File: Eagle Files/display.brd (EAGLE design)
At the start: 38.4 x 51.4 mm, 16 parts, among them CN1 Charger, IC1 ATMEGA 328P-PU

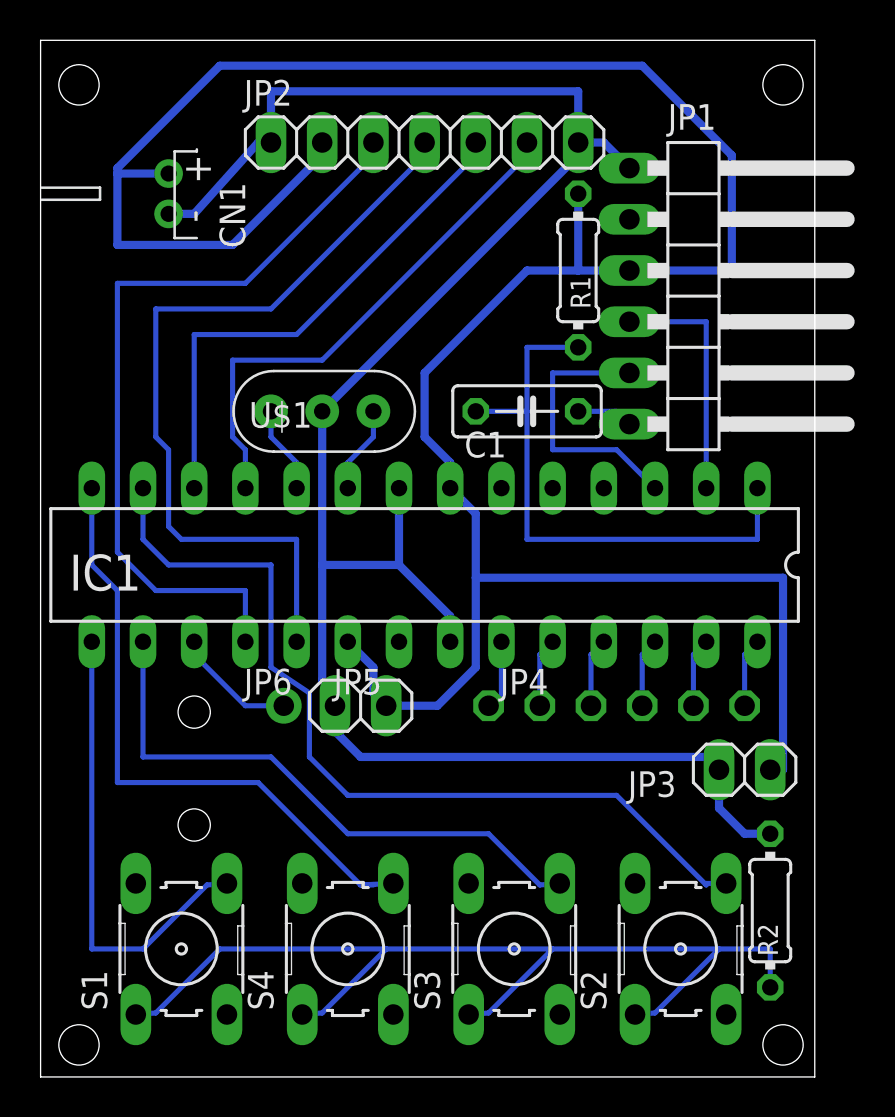
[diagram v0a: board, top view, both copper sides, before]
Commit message: removed one button
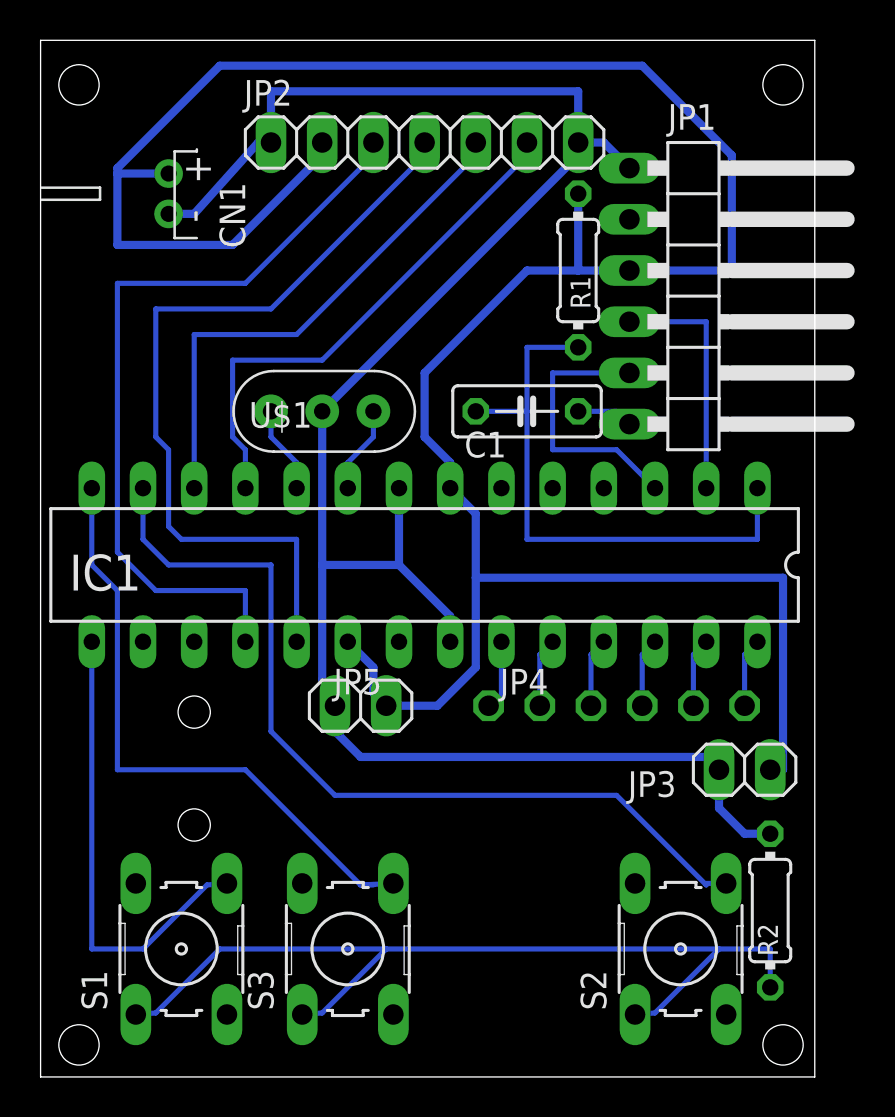
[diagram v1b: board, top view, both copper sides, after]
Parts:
- removed JP6: PWM, adafruit:1X01-CLEANBIG
- removed S4: (no value), switch-omron:B3F-10XX
- moved S3 8.26 mm to (15.2, 6.35)
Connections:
- removed net N$23: IC1.17, JP6.1
- removed net N$9: IC1.16, S3.4
- net N$13: no longer S4.1
- net N$17: now also S3.4; no longer S4.4
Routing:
- net N$9: track 29.0 -> 0.00 mm
- net N$23: track 6.13 -> 0.00 mm
- net N$13: track 51.1 -> 45.7 mm
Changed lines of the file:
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@@
 <attribute name="OC_FARNELL" value="176432" x="31.75" y="6.35" size="1.778" layer="27" rot="R90" display="off"/>
-</element>
-<element name="S3" library="switch-omron" package="B3F-10XX" value="" x="23.495" y="6.35" rot="R90">
-<attribute name="OC_NEWARK" value="36M3542" x="23.495" y="6.35" size="1.778" layer="27" rot="R90" display="off"/>
-<attribute name="MPN" value="B3F-1000" x="23.495" y="6.35" size="1.778" layer="27" rot="R90" display="off"/>
-<attribute name="MF" value="" x="23.495" y="6.35" size="1.778" layer="27" rot="R90" display="off"/>
-<attribute name="OC_FARNELL" value="176432" x="23.495" y="6.35" size="1.778" layer="27" rot="R90" display="off"/>
 </element>
 <element name="R2" library="rcl" package="0204/7" value="100" x="36.195" y="8.255" smashed="yes" rot="R270">
@@
 <attribute name="VALUE" x="35.7124" y="10.5156" size="0.9906" layer="27" ratio="10" rot="R270"/>
 </element>
-<element name="S4" library="switch-omron" package="B3F-10XX" value="" x="15.24" y="6.35" rot="R90">
+<element name="S3" library="switch-omron" package="B3F-10XX" value="" x="15.24" y="6.35" rot="R90">
 <attribute name="OC_NEWARK" value="36M3542" x="15.24" y="6.35" size="1.778" layer="27" rot="R90" display="off"/>
 <attribute name="MPN" value="B3F-1000" x="15.24" y="6.35" size="1.778" layer="27" rot="R90" display="off"/>
@@
 <attribute name="NAME" x="22.7838" y="18.9738" size="1.27" layer="25" ratio="10"/>
 <attribute name="VALUE" x="21.59" y="15.875" size="1.27" layer="27"/>
-</element>
-<element name="JP6" library="adafruit" package="1X01-CLEANBIG" value="PWM" x="12.065" y="18.415" smashed="yes">
-<attribute name="NAME" x="10.0838" y="18.9738" size="1.27" layer="25" ratio="10"/>
-<attribute name="VALUE" x="9.525" y="15.875" size="1.27" layer="27"/>
 </element>
 </elements>
@@
 <signal name="N$11">
 <contactref element="S2" pad="4"/>
-<wire x1="15.24" y1="13.97" x2="13.335" y2="15.875" width="0.254" layer="16"/>
-<wire x1="13.335" y1="15.875" x2="13.335" y2="19.05" width="0.254" layer="16"/>
-<wire x1="13.335" y1="19.05" x2="11.43" y2="20.32" width="0.254" layer="16"/>
-<wire x1="11.43" y1="20.32" x2="11.43" y2="25.4" width="0.254" layer="16"/>
-<wire x1="28.575" y1="13.97" x2="15.24" y2="13.97" width="0.254" layer="16"/>
+<wire x1="14.605" y1="13.97" x2="11.43" y2="17.145" width="0.254" layer="16"/>
+<wire x1="11.43" y1="17.145" x2="11.43" y2="25.4" width="0.254" layer="16"/>
+<wire x1="28.575" y1="13.97" x2="14.605" y2="13.97" width="0.254" layer="16"/>
 <wire x1="33.02" y1="9.525" x2="28.575" y2="13.97" width="0.254" layer="16"/>
 <wire x1="33.02" y1="9.525" x2="33.02" y2="9.6012" width="0.254" layer="16"/>
@@
 <wire x1="6.35" y1="25.4" x2="5.08" y2="26.67" width="0.254" layer="16"/>
 <wire x1="5.08" y1="26.67" x2="5.08" y2="29.21" width="0.254" layer="16"/>
-</signal>
-<signal name="N$9">
-<contactref element="S3" pad="4"/>
-<contactref element="IC1" pad="16"/>
-<wire x1="24.765" y1="9.525" x2="22.225" y2="12.065" width="0.254" layer="16"/>
-<wire x1="24.765" y1="9.525" x2="25.7556" y2="9.6012" width="0.254" layer="16"/>
-<wire x1="22.225" y1="12.065" x2="15.24" y2="12.065" width="0.254" layer="16"/>
-<wire x1="15.24" y1="12.065" x2="11.43" y2="15.875" width="0.254" layer="16"/>
-<wire x1="11.43" y1="15.875" x2="5.08" y2="15.875" width="0.254" layer="16"/>
-<wire x1="5.08" y1="15.875" x2="5.08" y2="21.59" width="0.254" layer="16"/>
 </signal>
 <signal name="N$4">
@@
 </signal>
 <signal name="N$13">
-<contactref element="S3" pad="1"/>
 <contactref element="R2" pad="2"/>
 <contactref element="S1" pad="1"/>
 <contactref element="S2" pad="1"/>
-<contactref element="S4" pad="1"/>
+<contactref element="S3" pad="1"/>
 <wire x1="17.145" y1="6.35" x2="13.97" y2="3.175" width="0.254" layer="16"/>
 <wire x1="13.97" y1="3.175" x2="12.9794" y2="3.0988" width="0.254" layer="16"/>
@@
 <wire x1="30.48" y1="3.175" x2="33.655" y2="6.35" width="0.254" layer="16"/>
 <wire x1="30.48" y1="3.175" x2="29.4894" y2="3.0988" width="0.254" layer="16"/>
-<wire x1="25.4" y1="6.35" x2="22.225" y2="3.175" width="0.254" layer="16"/>
-<wire x1="33.655" y1="6.35" x2="25.4" y2="6.35" width="0.254" layer="16"/>
-<wire x1="22.225" y1="3.175" x2="21.2344" y2="3.0988" width="0.254" layer="16"/>
-<wire x1="25.4" y1="6.35" x2="17.145" y2="6.35" width="0.254" layer="16"/>
+<wire x1="33.655" y1="6.35" x2="17.145" y2="6.35" width="0.254" layer="16"/>
 <wire x1="17.145" y1="6.35" x2="8.89" y2="6.35" width="0.254" layer="16"/>
 <wire x1="8.89" y1="6.35" x2="5.715" y2="3.175" width="0.254" layer="16"/>
@@
 </signal>
 <signal name="N$17">
-<contactref element="S4" pad="4"/>
+<contactref element="S3" pad="4"/>
 <contactref element="IC1" pad="14"/>
 <wire x1="2.54" y1="25.4" x2="2.54" y2="29.21" width="0.254" layer="16"/>
-<wire x1="10.795" y1="14.605" x2="3.81" y2="14.605" width="0.254" layer="16"/>
-<wire x1="3.81" y1="14.605" x2="3.81" y2="24.13" width="0.254" layer="16"/>
+<wire x1="10.16" y1="15.24" x2="3.81" y2="15.24" width="0.254" layer="16"/>
+<wire x1="3.81" y1="15.24" x2="3.81" y2="24.13" width="0.254" layer="16"/>
 <wire x1="3.81" y1="24.13" x2="2.54" y2="25.4" width="0.254" layer="16"/>
 <wire x1="16.51" y1="9.525" x2="15.875" y2="9.525" width="0.254" layer="16"/>
-<wire x1="15.875" y1="9.525" x2="10.795" y2="14.605" width="0.254" layer="16"/>
+<wire x1="15.875" y1="9.525" x2="10.16" y2="15.24" width="0.254" layer="16"/>
 <wire x1="15.875" y1="9.525" x2="17.5006" y2="9.6012" width="0.254" layer="16"/>
 </signal>
@@
 <wire x1="24.765" y1="18.415" x2="24.765" y2="20.955" width="0.254" layer="16"/>
 </signal>
-<signal name="N$23">
-<contactref element="IC1" pad="17"/>
-<wire x1="12.065" y1="18.415" x2="10.16" y2="18.415" width="0.254" layer="16"/>
-<wire x1="10.16" y1="18.415" x2="7.62" y2="20.955" width="0.254" layer="16"/>
-<wire x1="7.62" y1="20.955" x2="7.62" y2="21.59" width="0.254" layer="16"/>
-<contactref element="JP6" pad="1"/>
-</signal>
 <signal name="N$24">

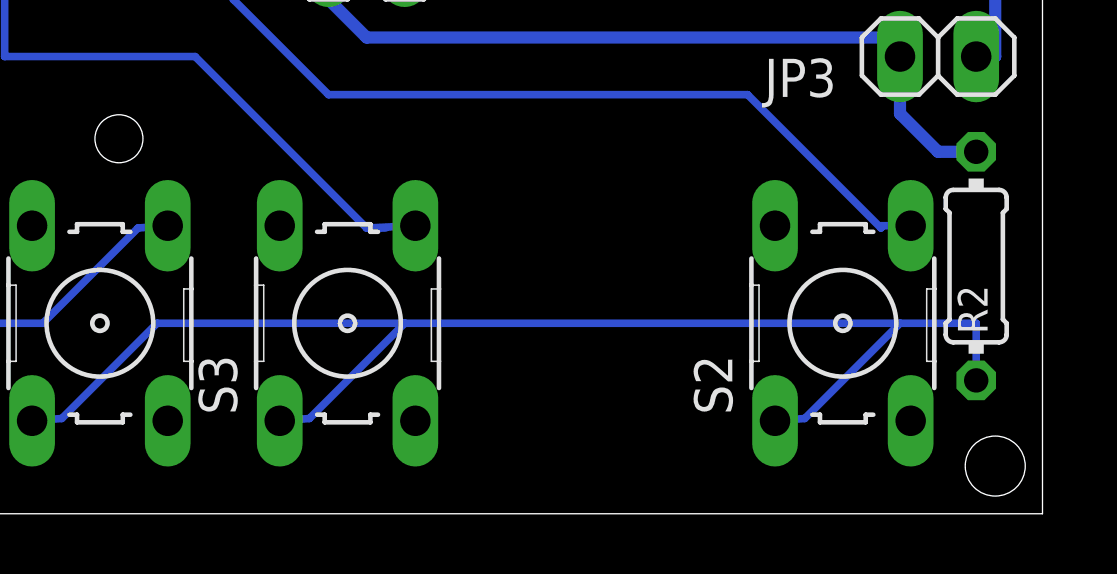
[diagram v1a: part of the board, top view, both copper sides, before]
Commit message: changed labes and positioning
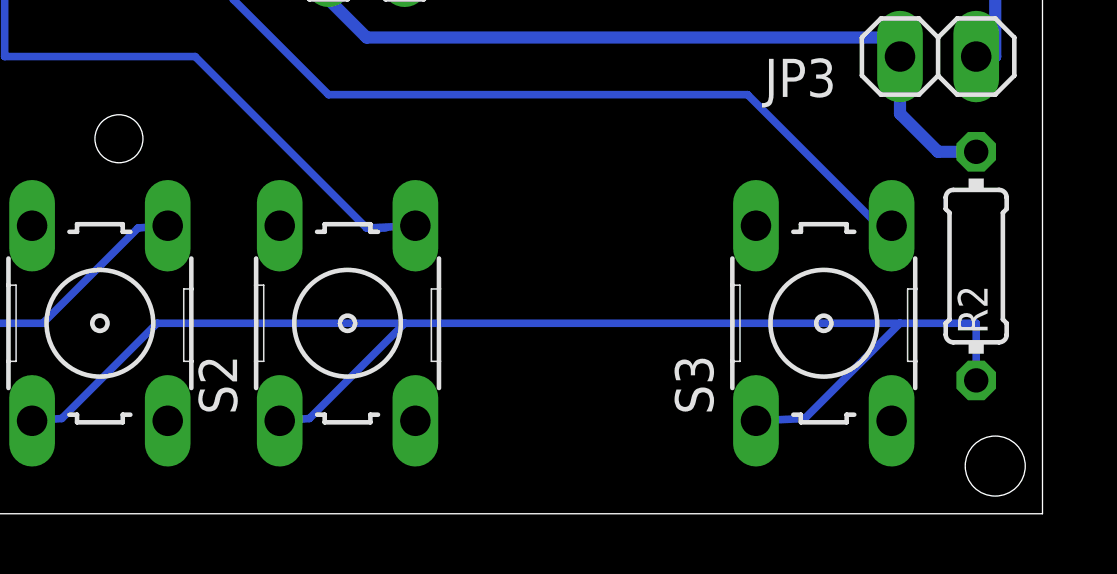
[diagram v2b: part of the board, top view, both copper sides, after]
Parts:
- moved S2 16.5 mm to (15.2, 6.35)
- moved S3 15.9 mm to (31.1, 6.35)
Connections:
- net N$11: now also S3.4; no longer S2.4
- net N$17: now also S2.4; no longer S3.4
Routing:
- net N$11: track 43.5 -> 42.8 mm
- net N$13: track 45.7 -> 46.3 mm
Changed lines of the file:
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@@
 <attribute name="OC_FARNELL" value="176432" x="6.985" y="6.35" size="1.778" layer="27" rot="R90" display="off"/>
 </element>
-<element name="S2" library="switch-omron" package="B3F-10XX" value="" x="31.75" y="6.35" rot="R90">
-<attribute name="OC_NEWARK" value="36M3542" x="31.75" y="6.35" size="1.778" layer="27" rot="R90" display="off"/>
-<attribute name="MPN" value="B3F-1000" x="31.75" y="6.35" size="1.778" layer="27" rot="R90" display="off"/>
-<attribute name="MF" value="" x="31.75" y="6.35" size="1.778" layer="27" rot="R90" display="off"/>
-<attribute name="OC_FARNELL" value="176432" x="31.75" y="6.35" size="1.778" layer="27" rot="R90" display="off"/>
+<element name="S3" library="switch-omron" package="B3F-10XX" value="" x="31.115" y="6.35" rot="R90">
+<attribute name="OC_NEWARK" value="36M3542" x="31.115" y="6.35" size="1.778" layer="27" rot="R90" display="off"/>
+<attribute name="MPN" value="B3F-1000" x="31.115" y="6.35" size="1.778" layer="27" rot="R90" display="off"/>
+<attribute name="MF" value="" x="31.115" y="6.35" size="1.778" layer="27" rot="R90" display="off"/>
+<attribute name="OC_FARNELL" value="176432" x="31.115" y="6.35" size="1.778" layer="27" rot="R90" display="off"/>
 </element>
 <element name="R2" library="rcl" package="0204/7" value="100" x="36.195" y="8.255" smashed="yes" rot="R270">
@@
 <attribute name="VALUE" x="35.7124" y="10.5156" size="0.9906" layer="27" ratio="10" rot="R270"/>
 </element>
-<element name="S3" library="switch-omron" package="B3F-10XX" value="" x="15.24" y="6.35" rot="R90">
+<element name="S2" library="switch-omron" package="B3F-10XX" value="" x="15.24" y="6.35" rot="R90">
 <attribute name="OC_NEWARK" value="36M3542" x="15.24" y="6.35" size="1.778" layer="27" rot="R90" display="off"/>
 <attribute name="MPN" value="B3F-1000" x="15.24" y="6.35" size="1.778" layer="27" rot="R90" display="off"/>
@@
 </signal>
 <signal name="N$11">
-<contactref element="S2" pad="4"/>
+<contactref element="S3" pad="4"/>
 <wire x1="14.605" y1="13.97" x2="11.43" y2="17.145" width="0.254" layer="16"/>
 <wire x1="11.43" y1="17.145" x2="11.43" y2="25.4" width="0.254" layer="16"/>
@@
 <wire x1="33.02" y1="9.525" x2="28.575" y2="13.97" width="0.254" layer="16"/>
 <wire x1="33.02" y1="9.525" x2="33.02" y2="9.6012" width="0.254" layer="16"/>
-<wire x1="33.02" y1="9.6012" x2="34.0106" y2="9.6012" width="0.254" layer="16"/>
+<wire x1="33.02" y1="9.6012" x2="33.3756" y2="9.6012" width="0.254" layer="16"/>
 <contactref element="IC1" pad="13"/>
 <wire x1="11.43" y1="25.4" x2="6.35" y2="25.4" width="0.254" layer="16"/>
@@
 <contactref element="R2" pad="2"/>
 <contactref element="S1" pad="1"/>
+<contactref element="S3" pad="1"/>
 <contactref element="S2" pad="1"/>
-<contactref element="S3" pad="1"/>
 <wire x1="17.145" y1="6.35" x2="13.97" y2="3.175" width="0.254" layer="16"/>
 <wire x1="13.97" y1="3.175" x2="12.9794" y2="3.0988" width="0.254" layer="16"/>
@@
 <wire x1="36.195" y1="6.35" x2="36.195" y2="4.445" width="0.254" layer="16"/>
 <wire x1="30.48" y1="3.175" x2="33.655" y2="6.35" width="0.254" layer="16"/>
-<wire x1="30.48" y1="3.175" x2="29.4894" y2="3.0988" width="0.254" layer="16"/>
+<wire x1="30.48" y1="3.175" x2="28.8544" y2="3.0988" width="0.254" layer="16"/>
 <wire x1="33.655" y1="6.35" x2="17.145" y2="6.35" width="0.254" layer="16"/>
 <wire x1="17.145" y1="6.35" x2="8.89" y2="6.35" width="0.254" layer="16"/>
@@
 </signal>
 <signal name="N$17">
-<contactref element="S3" pad="4"/>
+<contactref element="S2" pad="4"/>
 <contactref element="IC1" pad="14"/>
 <wire x1="2.54" y1="25.4" x2="2.54" y2="29.21" width="0.254" layer="16"/>
